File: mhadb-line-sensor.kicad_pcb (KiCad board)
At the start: 2 copper layers, 100 x 20 mm, 105 parts, among them J1 TC2030, J2 Conn_01x04_Pin, J3 Conn_01x04, J4 Conn_01x04_Pin, SW1 SW_Push, SW2 SW_Push, SW3 SW_Push, SW4 SW_Push, U1 HT753-1, U10 QRE1113GR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

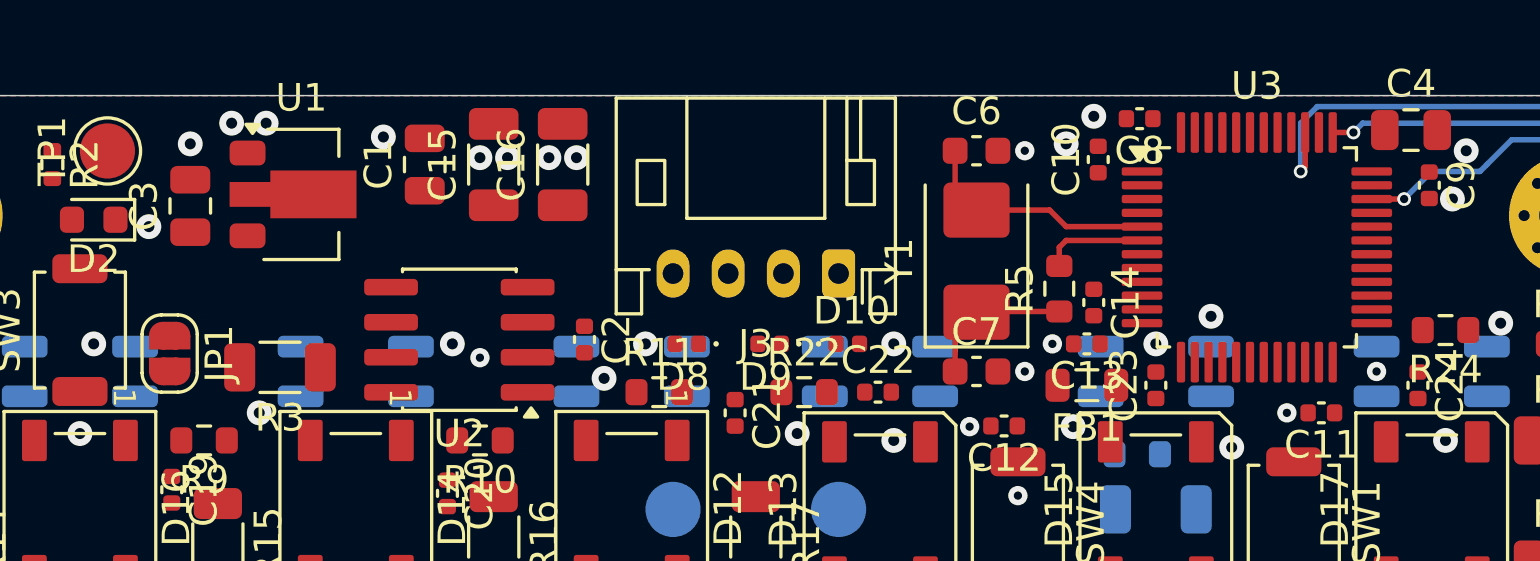
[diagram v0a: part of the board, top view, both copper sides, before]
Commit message: pcb: add CAN routing
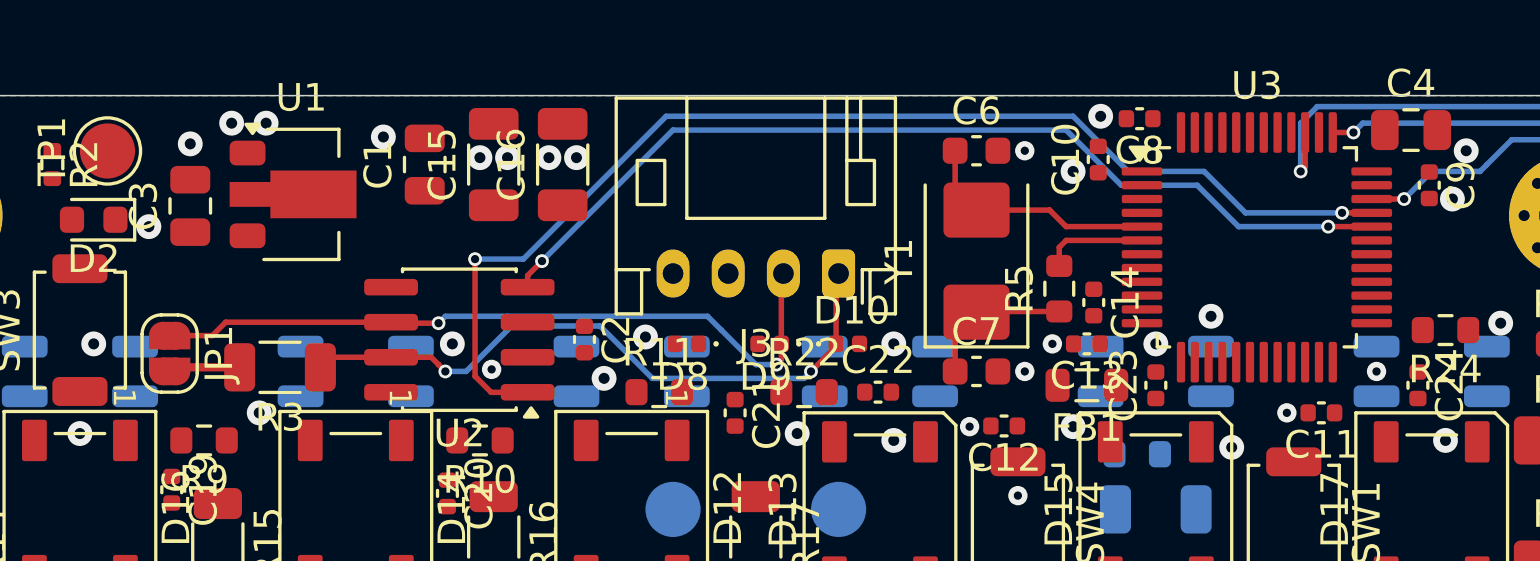
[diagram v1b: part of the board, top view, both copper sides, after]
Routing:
- net /CAN_TX: track 0.00 -> 42.5 mm, vias 0 -> 2
- net /CAN_RX: track 0.00 -> 34.7 mm, vias 0 -> 2
- net /CANL: track 0.00 -> 26.4 mm, vias 0 -> 2
- net /CANH: track 0.00 -> 23.7 mm, vias 0 -> 2
- net Net-(JP1-B): track 0.00 -> 2.60 mm

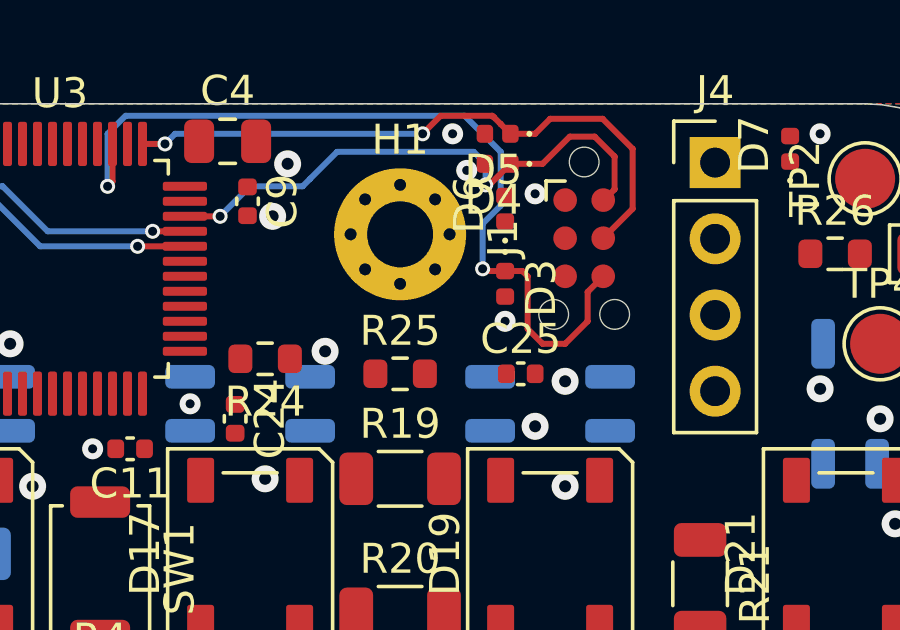
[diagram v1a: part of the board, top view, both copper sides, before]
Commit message: pcb: add UART routing
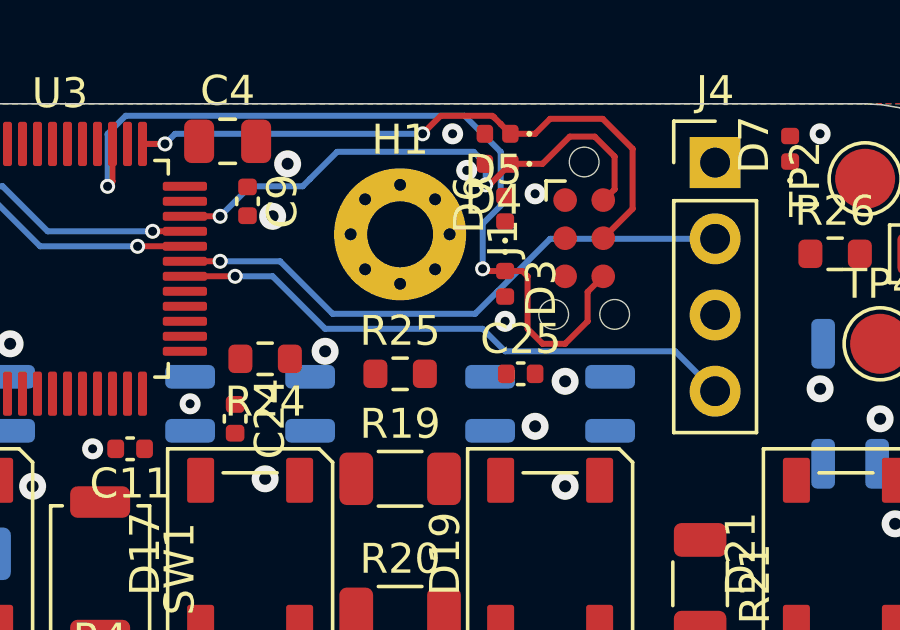
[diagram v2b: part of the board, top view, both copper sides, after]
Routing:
- net /U0RXD: track 0.00 -> 19.4 mm, vias 0 -> 1
- net /U0TXD: track 0.00 -> 19.3 mm, vias 0 -> 1
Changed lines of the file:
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@@
+	)
+	(segment
+		(start 182.5 89.25)
+		(end 181.325 89.25)
+		(width 0.2)
+		(layer "F.Cu")
+		(net 42)
+	)
+	(via
+		(at 182.5 89.25)
+		(size 0.5)
+		(drill 0.3)
+		(layers "F.Cu" "B.Cu")
+		(net 42)
+	)
+	(segment
+		(start 184.5 89.25)
+		(end 182.5 89.25)
+		(width 0.2)
+		(layer "B.Cu")
+		(net 42)
+	)
+	(segment
+		(start 186.25 91)
+		(end 184.5 89.25)
+		(width 0.2)
+		(layer "B.Cu")
+		(net 42)
+	)
+	(segment
+		(start 199 88.5)
+		(end 193.5 88.5)
+		(width 0.2)
+		(layer "B.Cu")
+		(net 42)
+	)
+	(segment
+		(start 193.5 88.5)
+		(end 191.75 90.25)
+		(width 0.2)
+		(layer "B.Cu")
+		(net 42)
+	)
+	(segment
+		(start 191.75 90.25)
+		(end 191 91)
+		(width 0.2)
+		(layer "B.Cu")
+		(net 42)
+	)
+	(segment
+		(start 191 91)
+		(end 188.5 91)
+		(width 0.2)
+		(layer "B.Cu")
+		(net 42)
+	)
+	(segment
+		(start 188.5 91)
+		(end 186.25 91)
+		(width 0.2)
+		(layer "B.Cu")
+		(net 42)
+	)
+	(segment
+		(start 181.325 89.75)
+		(end 183 89.75)
+		(width 0.2)
+		(layer "F.Cu")
+		(net 43)
+	)
+	(via
+		(at 183 89.75)
+		(size 0.5)
+		(drill 0.3)
+		(layers "F.Cu" "B.Cu")
+		(net 43)
+	)
+	(segment
+		(start 191.25 91.5)
+		(end 192 92.25)
+		(width 0.2)
+		(layer "B.Cu")
+		(net 43)
+	)
+	(segment
+		(start 183 89.75)
+		(end 184.25 89.75)
+		(width 0.2)
+		(layer "B.Cu")
+		(net 43)
+	)
+	(segment
+		(start 197.67 92.25)
+		(end 199 93.58)
+		(width 0.2)
+		(layer "B.Cu")
+		(net 43)
+	)
+	(segment
+		(start 184.25 89.75)
+		(end 186 91.5)
+		(width 0.2)
+		(layer "B.Cu")
+		(net 43)
+	)
+	(segment
+		(start 192 92.25)
+		(end 197.67 92.25)
+		(width 0.2)
+		(layer "B.Cu")
+		(net 43)
+	)
+	(segment
+		(start 186 91.5)
+		(end 191.25 91.5)
+		(width 0.2)
+		(layer "B.Cu")
+		(net 43)
 	)
 	(segment

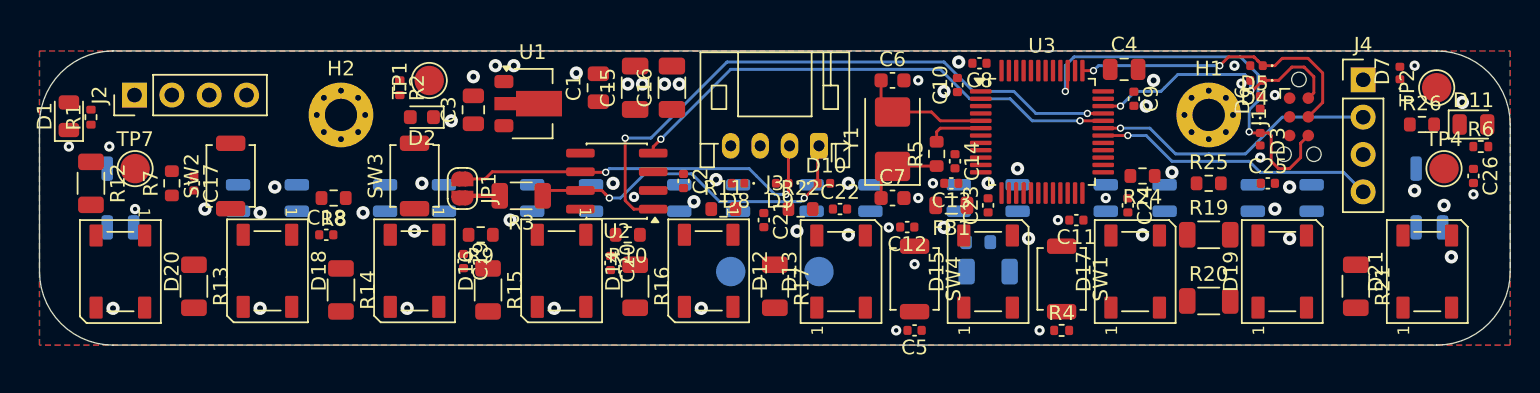
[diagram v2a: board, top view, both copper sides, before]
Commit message: pcb: add QRE1113 collectors routing
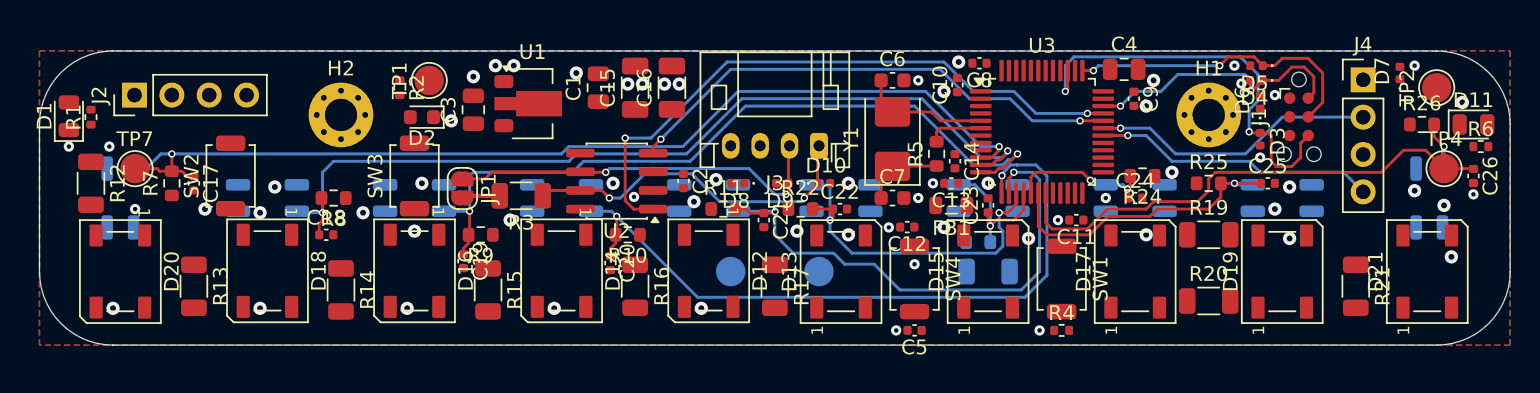
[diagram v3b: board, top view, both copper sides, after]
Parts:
- moved C24 0.71 mm to (183.5, 94.0), turned to 0 degrees
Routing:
- net /LS1: track 0.00 -> 69.7 mm, vias 0 -> 2
- net /LS2: track 0.00 -> 60.0 mm, vias 0 -> 2
- net /LS3: track 0.00 -> 51.6 mm, vias 0 -> 2
- net /LS4: track 0.00 -> 48.6 mm, vias 0 -> 2
- net /LS10: track 0.00 -> 40.3 mm, vias 0 -> 1
- net /LS5: track 0.00 -> 36.8 mm, vias 0 -> 2
- net /LS6: track 0.00 -> 23.6 mm, vias 0 -> 2
- net /LS9: track 0.00 -> 20.9 mm, vias 0 -> 1
- net /LS7: track 0.00 -> 10.3 mm, vias 0 -> 1
- net /LS8: track 0.00 -> 9.87 mm, vias 0 -> 2
- net GND: vias 63 -> 62

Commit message: pcb: add RGB leds routing
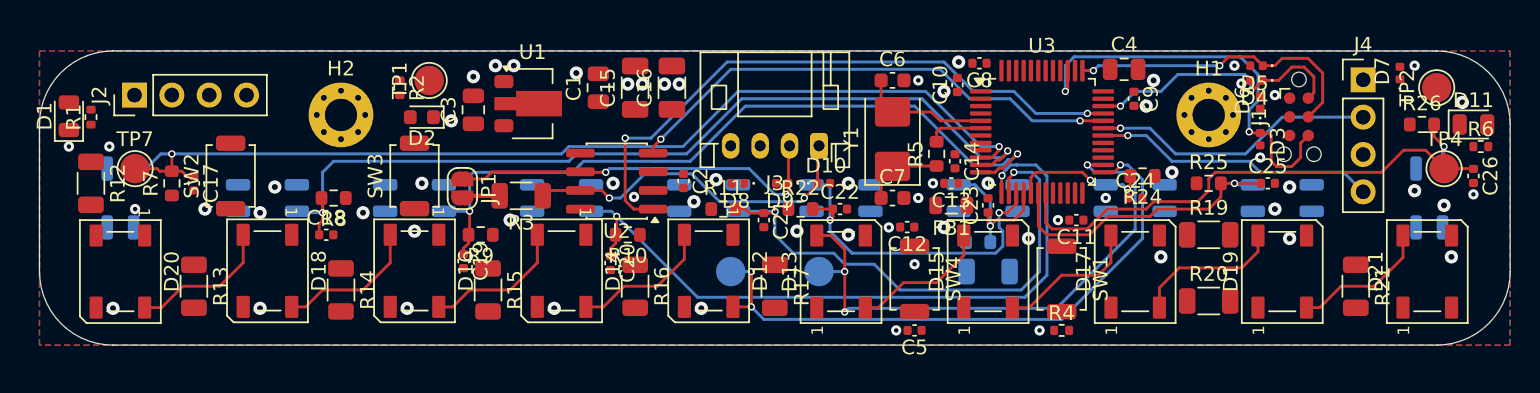
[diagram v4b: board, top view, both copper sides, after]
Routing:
- net /RGB1: track 0.00 -> 41.6 mm, vias 0 -> 3
- net /RGB2: track 0.00 -> 38.4 mm, vias 0 -> 3
- net Net-(D17-DOUT): track 0.00 -> 10.2 mm
- net Net-(D18-DOUT): track 0.00 -> 9.86 mm
- net Net-(D16-DOUT): track 0.00 -> 9.84 mm
- net Net-(D14-DOUT): track 0.00 -> 9.84 mm
- net Net-(D15-DOUT): track 0.00 -> 9.81 mm
- net Net-(D12-DOUT): track 0.00 -> 9.70 mm
- net Net-(D13-DOUT): track 0.00 -> 9.52 mm
- net Net-(D19-DOUT): track 0.00 -> 9.46 mm

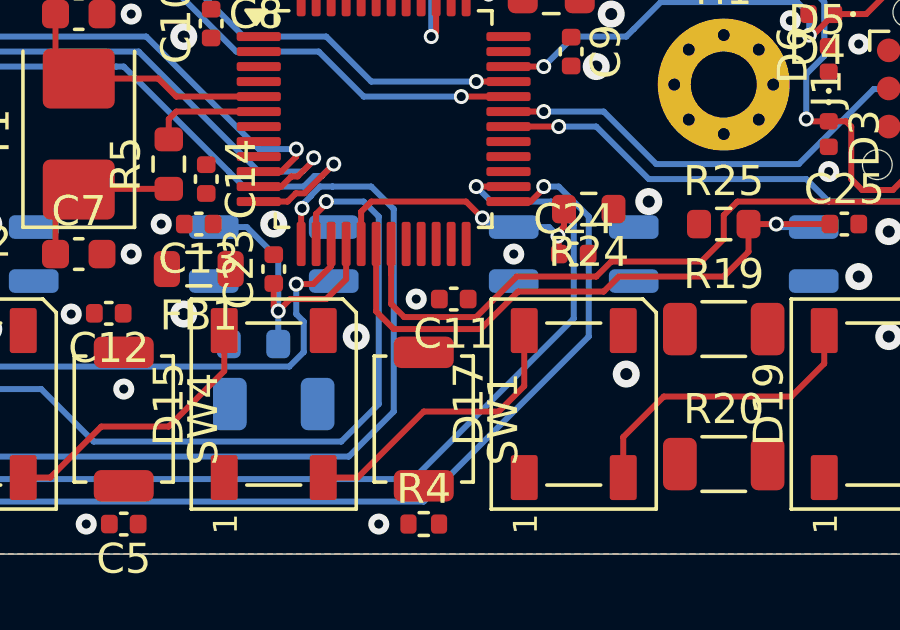
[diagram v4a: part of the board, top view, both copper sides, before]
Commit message: schem/pcb: add BOOT1 strapping
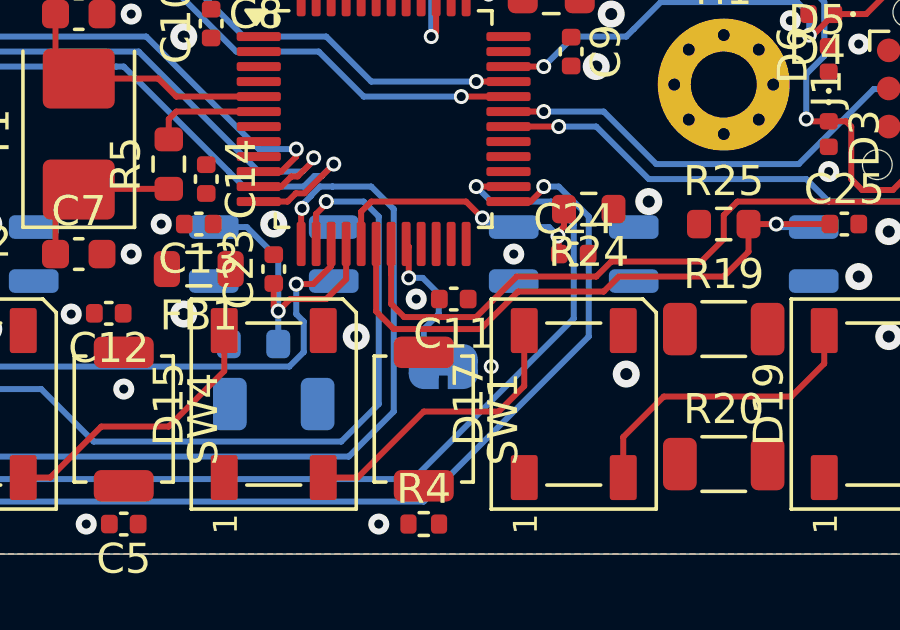
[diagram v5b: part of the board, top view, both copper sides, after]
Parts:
- added JP2: Jumper_2_Small_Bridged, Jumper:SolderJumper-2_P1.3mm_Bridged_RoundedPad1.0x1.5mm, B.Cu at (179.2, 97.8)
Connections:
- U3 pad 20: unconnected-(U3-PB2-Pad20) -> Net-(JP2-B)
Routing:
- net Net-(JP2-B): track 0.00 -> 5.02 mm, vias 0 -> 1
- net GND: vias 62 -> 63

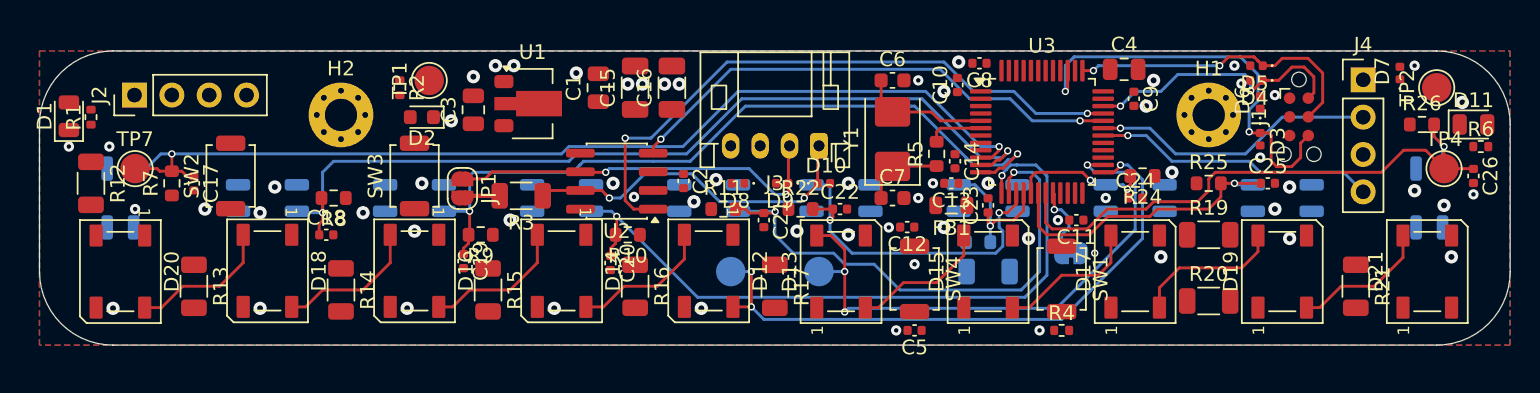
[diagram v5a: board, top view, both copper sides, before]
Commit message: pcb: add QRE1113 emitters routing
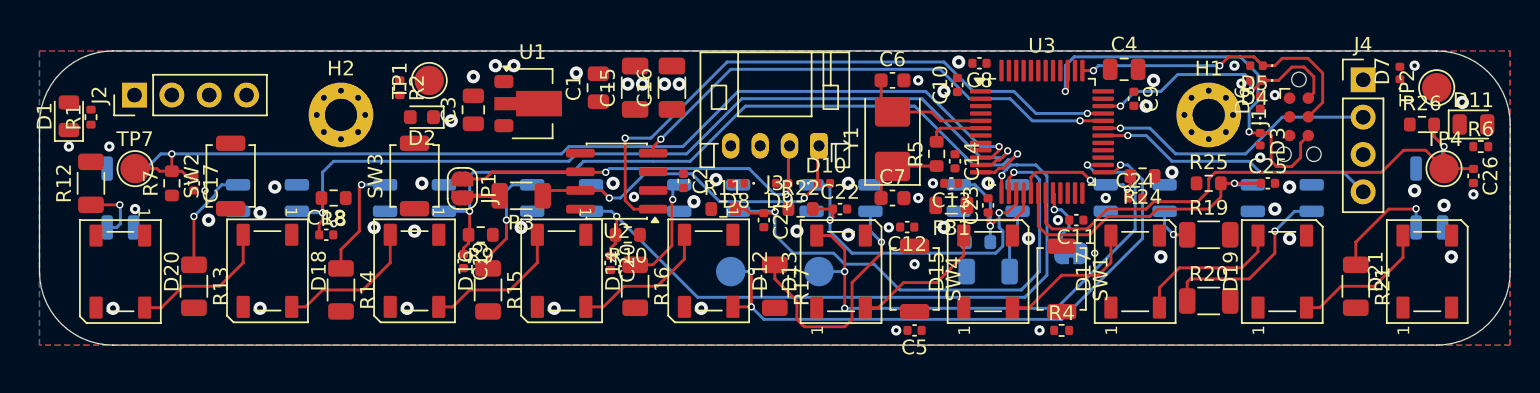
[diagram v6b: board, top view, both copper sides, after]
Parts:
- turned R12 to 90 degrees
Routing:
- net Net-(U9-A): track 0.00 -> 17.0 mm, vias 0 -> 1
- net Net-(U12-A): track 0.00 -> 12.6 mm, vias 0 -> 1
- net Net-(U6-A): track 0.00 -> 7.87 mm, vias 0 -> 1
- net Net-(U13-A): track 0.00 -> 7.85 mm, vias 0 -> 1
- net Net-(U7-A): track 0.00 -> 7.72 mm, vias 0 -> 1
- net Net-(U8-A): track 0.00 -> 7.45 mm, vias 0 -> 1
- net Net-(U5-A): track 0.00 -> 7.32 mm, vias 0 -> 1
- net Net-(U10-A): track 0.00 -> 4.32 mm
- net Net-(U4-A): track 0.00 -> 4.27 mm, vias 0 -> 1
- net Net-(U11-A): track 0.00 -> 2.98 mm, vias 0 -> 1
- net GND: vias 63 -> 65

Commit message: pcb: add 3v3 routing
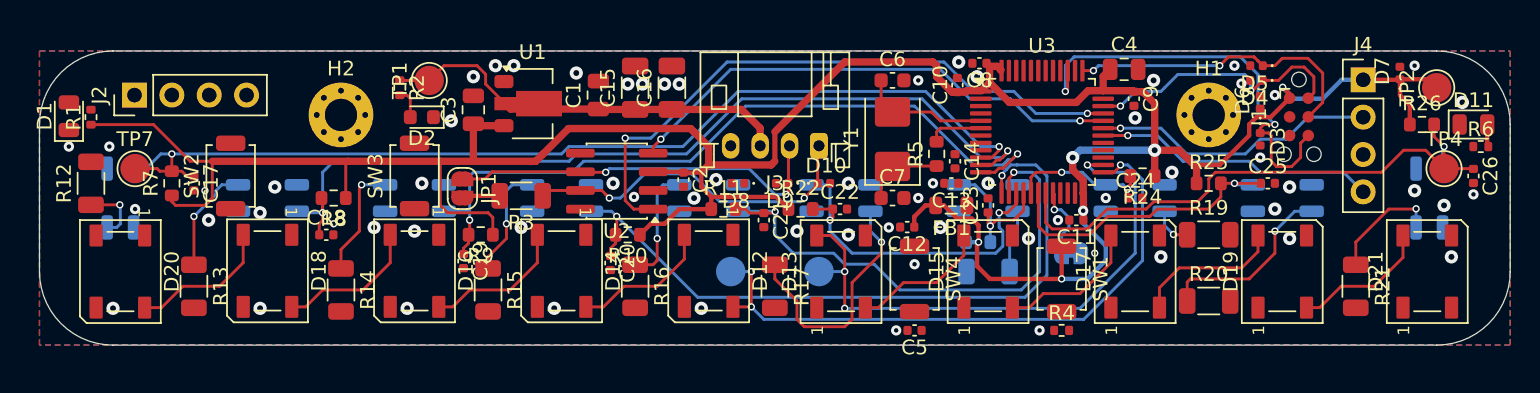
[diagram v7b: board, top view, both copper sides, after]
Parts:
- moved C1 0.50 mm to (147.0, 87.0)
- moved C2 0.09 mm to (152.8, 92.8)
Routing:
- net +3V3: track 0.00 -> 195.9 mm, vias 0 -> 6
- net +5V: track 0.00 -> 28.3 mm
- net Net-(D2-A): track 0.00 -> 2.07 mm
- net Net-(D11-A): track 0.00 -> 1.53 mm
- net /RGB2: track 38.0 -> 38.9 mm
- net /RGB1: track 41.6 -> 42.5 mm
- net Net-(U8-A): track 7.45 -> 8.03 mm

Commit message: pcb: add 5v routing
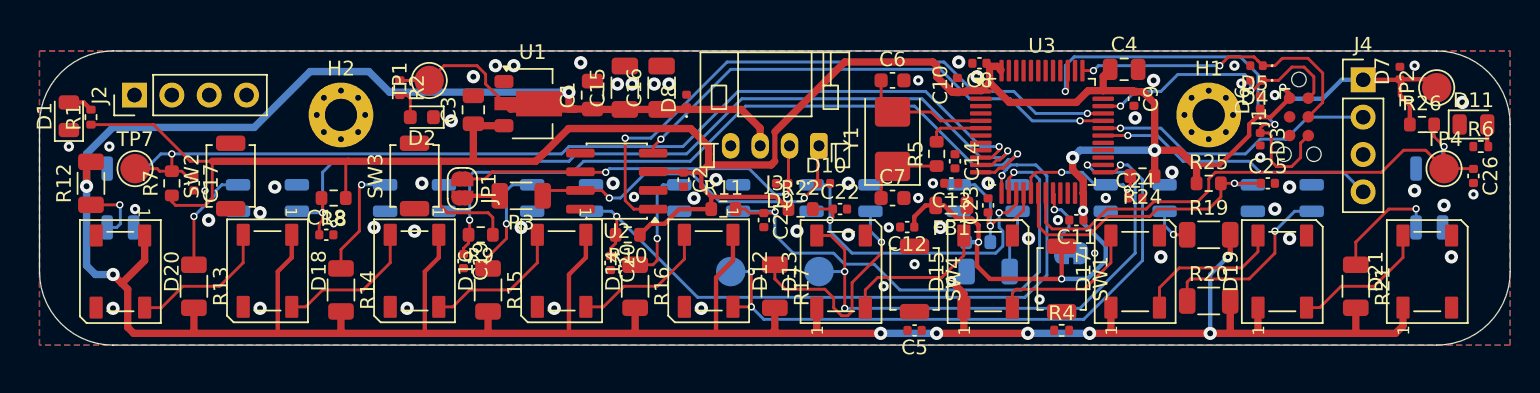
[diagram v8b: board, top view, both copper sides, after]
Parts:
- moved D8 6.60 mm to (153.0, 87.4), turned to 90 degrees
- moved C15 0.70 mm to (148.8, 86.5)
- moved C16 0.70 mm to (151.3, 86.5)
- moved C1 0.40 mm to (146.6, 87.0)
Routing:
- net +5V: track 28.3 -> 232.1 mm, vias 0 -> 10
- net Net-(D1-A): track 0.00 -> 1.70 mm
- net Net-(U9-A): track 17.0 -> 15.7 mm
- net Net-(D13-DOUT): track 9.52 -> 10.2 mm
- net Net-(D15-DOUT): track 9.81 -> 10.4 mm
